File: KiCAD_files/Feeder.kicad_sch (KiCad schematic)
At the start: 82 parts, among them J405 Conn_01x02_Male, J406 Conn_01x02_Male, J501 Conn_01x03, Q501 60V N channel, Q502 TK13P25D,RQ, T501 PA2467NL, U407 OPA316, U501 NCP12700, U503 TL431MFDT,215

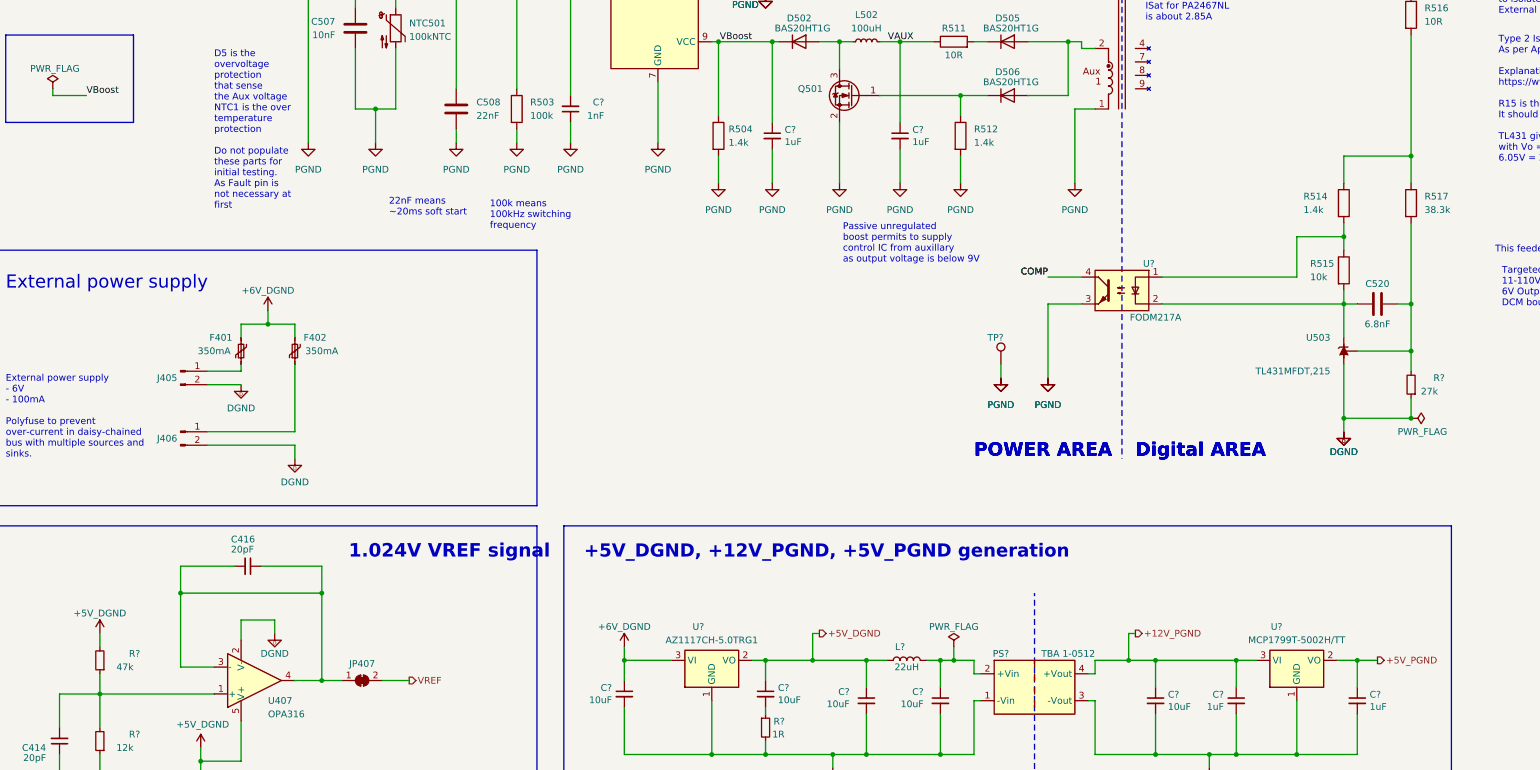
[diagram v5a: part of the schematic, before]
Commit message: synchronized PCB to schematic to have latest schematic value update on PCB and generated new ibom
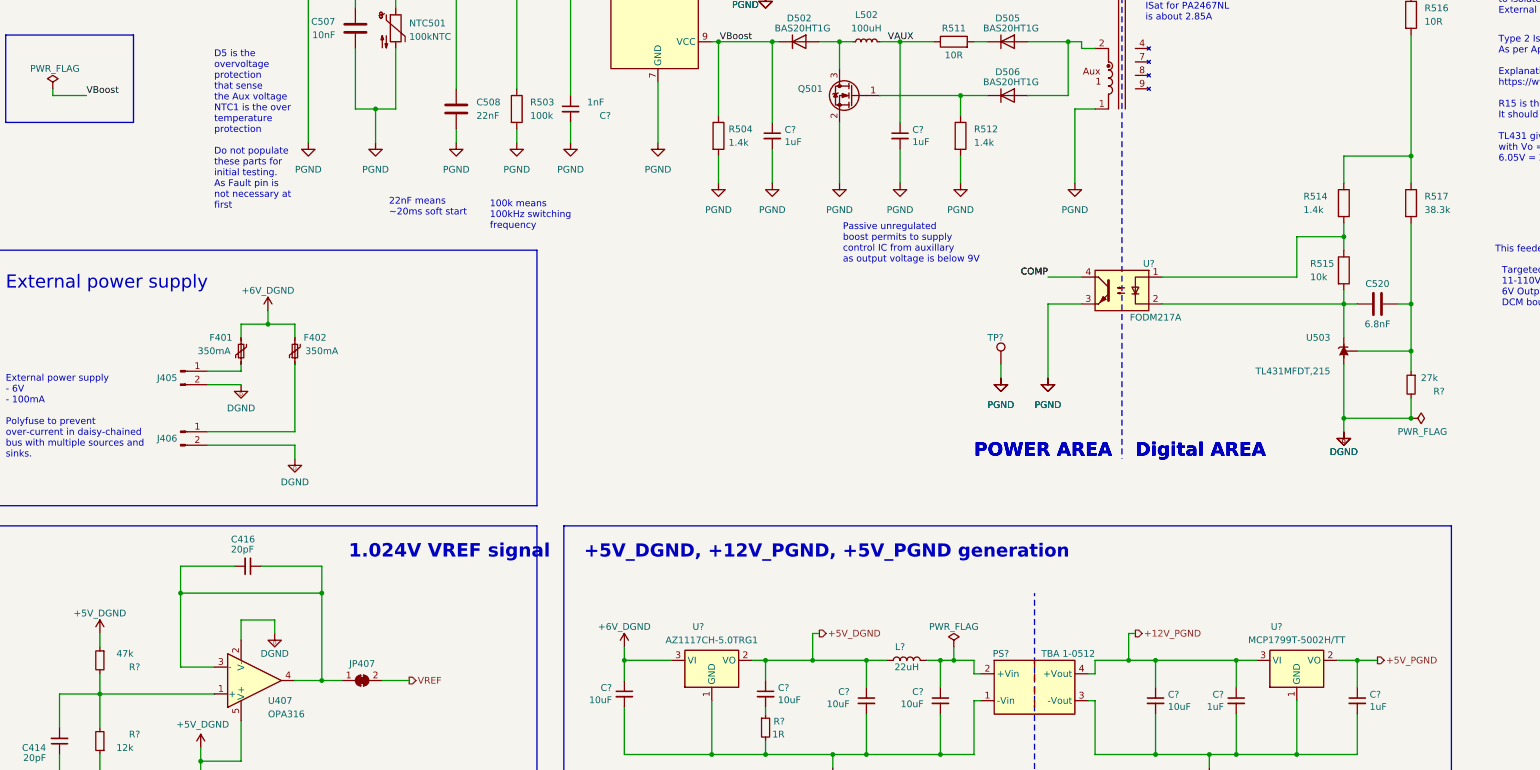
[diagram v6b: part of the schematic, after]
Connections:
- net +5V_DGND: now also R?.1; no longer R?.2
- net COMP: now also C?.1; no longer C?.2
- net DGND: now also R?.2; no longer R?.1
- net PGND: now also C?.2; no longer C?.1
- net at C520.2, R517.2, U503.2 (REF): now also R?.1; no longer R?.2
- net at C414.2, R?.2, U407.1 (+): now also R?.2; no longer R?.1
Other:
- moved on the sheet: C?, R?
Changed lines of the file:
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@@
     )
   )
-  (symbol (lib_name "R_Small_14") (lib_id "Device:R_Small") (at 285.75 191.77 180) (unit 1)
-    (in_bom yes) (on_board yes) (dnp no)
-    (property "Reference" "R?" (at 292.1 190.5 0)
-      (effects (font (size 1.27 1.27)) (justify left))
-    )
-    (property "Value" "27k" (at 290.83 193.04 0)
+  (symbol (lib_name "R_Small_14") (lib_id "Device:R_Small") (at 285.75 191.77 0) (mirror y) (unit 1)
+    (in_bom yes) (on_board yes) (dnp no)
+    (property "Reference" "R?" (at 292.1 193.04 0)
+      (effects (font (size 1.27 1.27)) (justify left))
+    )
+    (property "Value" "27k" (at 290.83 190.5 0)
       (effects (font (size 1.27 1.27)) (justify left))
     )
@@
     )
   )
-  (symbol (lib_id "Device:C_Small") (at 127 139.7 180) (unit 1)
-    (in_bom yes) (on_board yes) (dnp no)
-    (property "Reference" "C?" (at 133.35 138.43 0)
-      (effects (font (size 1.27 1.27)) (justify left))
-    )
-    (property "Value" "1nF" (at 133.35 140.97 0)
+  (symbol (lib_id "Device:C_Small") (at 127 139.7 0) (mirror y) (unit 1)
+    (in_bom yes) (on_board yes) (dnp no)
+    (property "Reference" "C?" (at 134.62 140.97 0)
+      (effects (font (size 1.27 1.27)) (justify left))
+    )
+    (property "Value" "1nF" (at 133.35 138.43 0)
       (effects (font (size 1.27 1.27)) (justify left))
     )
@@
       (effects (font (size 1.27 1.27)) hide)
     )
-    (property "Package" "0805" (at 132.08 144.78 0)
-      (effects (font (size 1.27 1.27)) hide)
-    )
-    (property "Voltage" "100V" (at 132.08 142.24 0)
+    (property "Package" "0805" (at 132.08 134.62 0)
+      (effects (font (size 1.27 1.27)) hide)
+    )
+    (property "Voltage" "100V" (at 132.08 137.16 0)
       (effects (font (size 1.27 1.27)) hide)
     )
@@
     )
   )
-  (symbol (lib_id "Device:R_Small") (at 38.1 243.84 180) (unit 1)
-    (in_bom yes) (on_board yes) (dnp no)
-    (property "Reference" "R?" (at 45.72 242.57 0)
-      (effects (font (size 1.27 1.27)) (justify left))
-    )
-    (property "Value" "47k" (at 44.45 245.11 0)
-      (effects (font (size 1.27 1.27)) (justify left))
-    )
+  (symbol (lib_id "Device:R_Small") (at 38.1 243.84 0) (mirror y) (unit 1)
+    (in_bom yes) (on_board yes) (dnp no)
+    (property "Reference" "R?" (at 45.72 245.11 0)
+      (effects (font (size 1.27 1.27)) (justify left))
+    )
+    (property "Value" "47k" (at 44.45 242.57 0)
+      (effects (font (size 1.27 1.27)) (justify left))
+    )

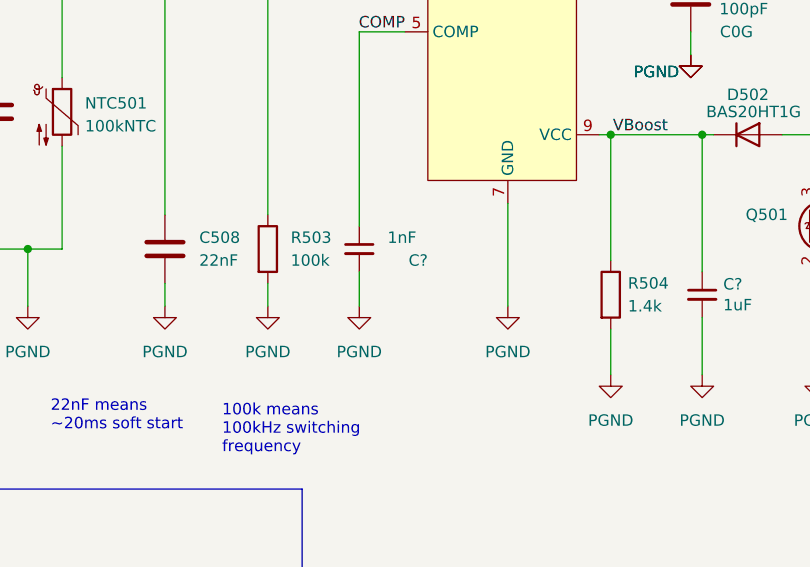
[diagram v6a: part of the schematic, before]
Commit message: minor modifications to components field for better schematic reading
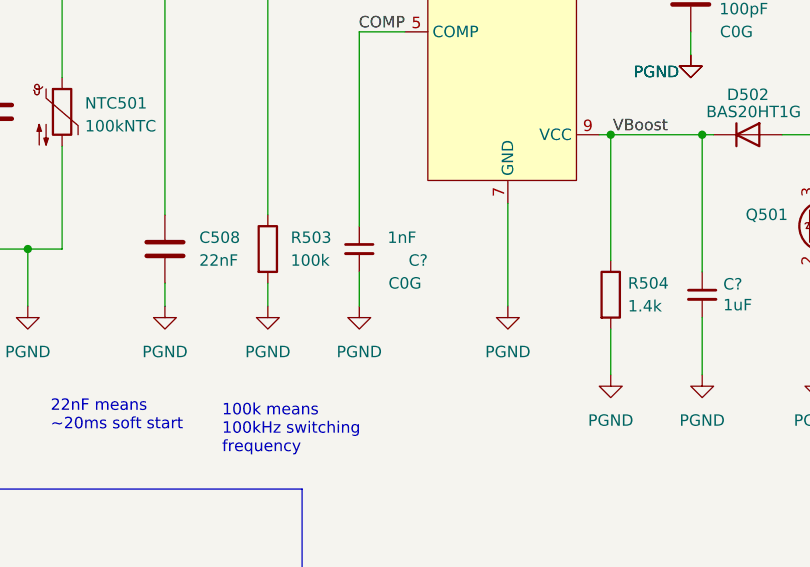
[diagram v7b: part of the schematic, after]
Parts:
- C?: Dielectric (none) -> C0G
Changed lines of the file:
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@@
       (effects (font (size 1.27 1.27)) hide)
+    )
+    (property "Dielectric" "C0G" (at 132.08 143.51 0)
+      (effects (font (size 1.27 1.27)))
     )
     (pin "1")

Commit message: update manf after fab of two first boards
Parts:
- F402: manf# 0ZCJ0050AF2E -> 0ZCH0035FF2G
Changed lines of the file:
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@@
       (effects (font (size 1.27 1.27)) hide)
     )
-    (property "manf#" "0ZCJ0050AF2E" (at 74.93 185.42 0)
+    (property "manf#" "0ZCH0035FF2G" (at 74.93 185.42 0)
       (effects (font (size 1.27 1.27)) hide)
     )
